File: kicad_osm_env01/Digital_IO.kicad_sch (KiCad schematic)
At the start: 4 parts

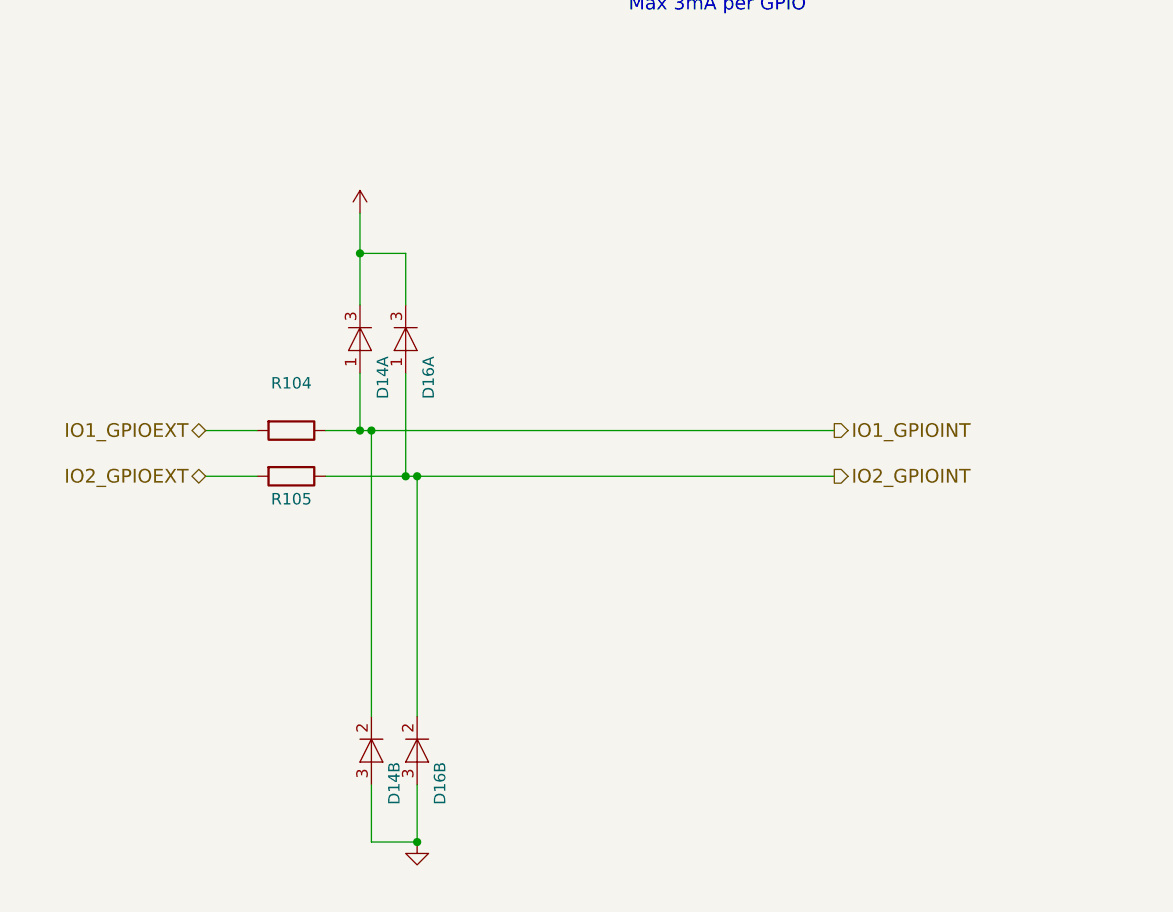
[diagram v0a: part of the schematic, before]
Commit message: added stml433 to schematic and carried out some mods
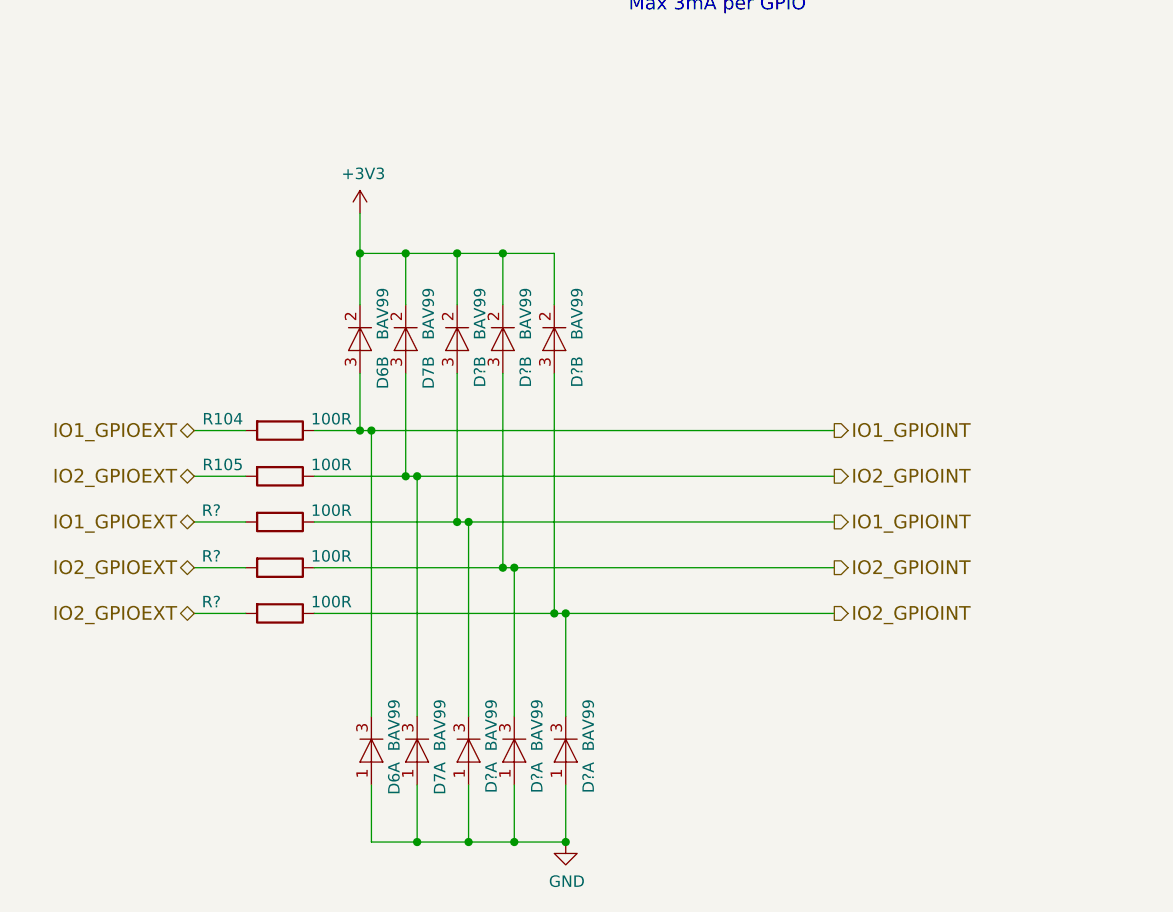
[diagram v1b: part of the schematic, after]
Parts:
- added D? (x6): BAV99, Package_TO_SOT_SMD:SOT-23, symbol OSM_env01-rescue:BAV99-Diode-ESP32-EVB_Rev_D-rescue
- added R? (x3): 100R, Resistor_SMD:R_0603_1608Metric, symbol OSM_env01-rescue:R-device-ESP32-EVB_Rev_D-rescue
- D6: renamed from D14; value (none) -> BAV99; footprint (none) -> Package_TO_SOT_SMD:SOT-23
- D7: renamed from D16; value (none) -> BAV99; footprint (none) -> Package_TO_SOT_SMD:SOT-23
- R104, R105: value (none) -> 100R; footprint (none) -> Resistor_SMD:R_0603_1608Metric
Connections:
- net +3V3: now also D6.2 (K), D7.2 (K), D?.2 (K), D?.2 (K), D?.2 (K); no longer D6.3 (K), D7.3 (K)
- net GND: now also D6.1 (A), D7.1 (A), D?.1 (A), D?.1 (A), D?.1 (A); no longer D6.3 (A), D7.3 (A)
- net IO1_GPIOEXT: now also R?.2
- net IO1_GPIOINT: now also D6.3 (A), D6.3 (K), D?.3 (A), D?.3 (K), R?.1; no longer D6.1 (A), D6.2 (K)
- net IO2_GPIOEXT: now also R?.2, R?.2
- net IO2_GPIOINT: now also D7.3 (A), D7.3 (K), D?.3 (A), D?.3 (A), D?.3 (K), D?.3 (K), R?.1, R?.1; no longer D7.1 (A), D7.2 (K)
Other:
- moved on the sheet: R104, R105

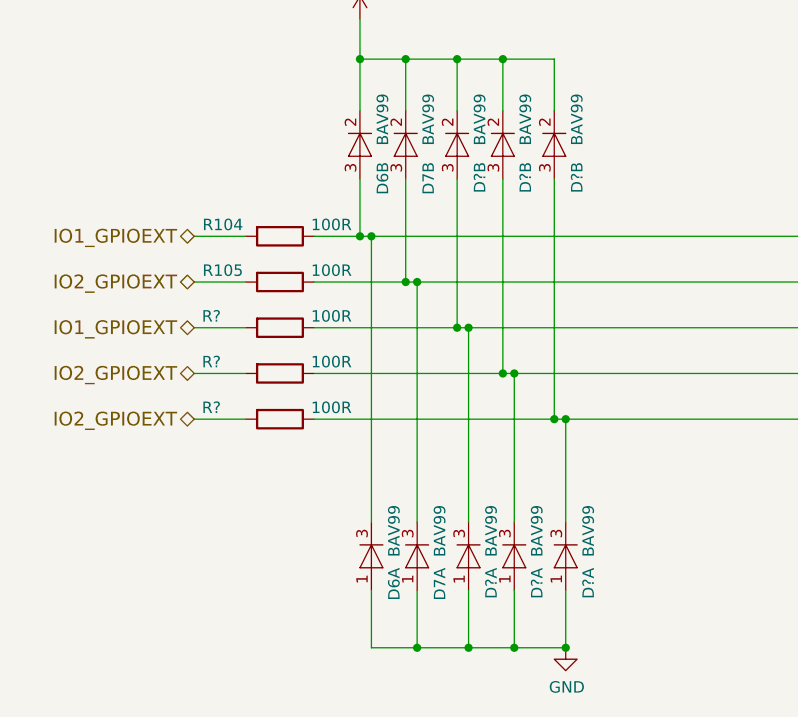
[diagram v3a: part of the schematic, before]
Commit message: added new battery charge ic u2
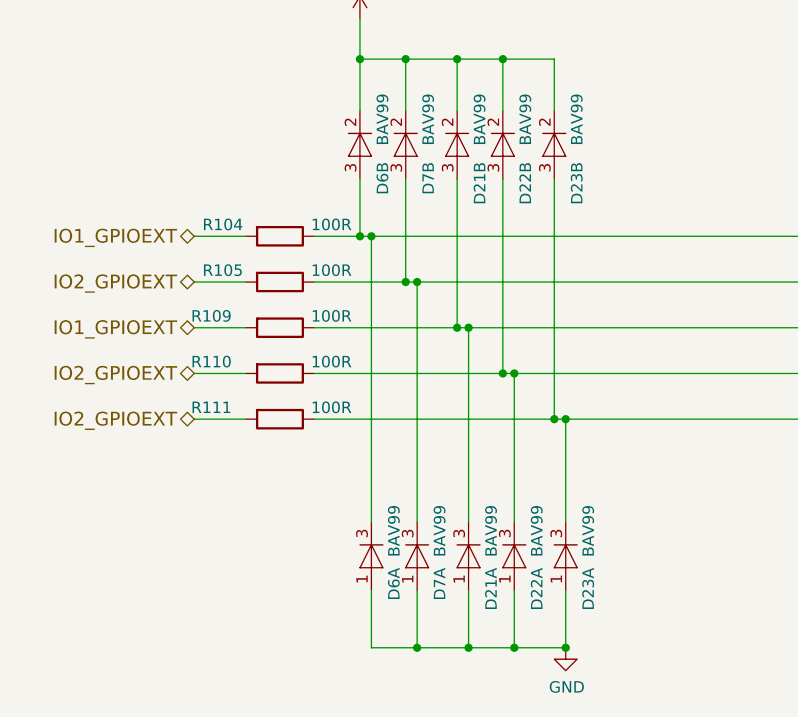
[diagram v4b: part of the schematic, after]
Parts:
- gave numbers to parts that had none: 6
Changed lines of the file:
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@@
   (title_block
     (title "Open Smart Monitor")
-    (date "2021-09-29")
-    (rev "B")
+    (date "2022-07-01")
+    (rev "C")
     (company "Devtank LTD")
     (comment 1 "Part No: 304-010")
@@
   (symbol (lib_id "OSM_env01:GND") (at 119.38 139.065 0) (unit 1)
     (in_bom yes) (on_board yes)
-    (property "Reference" "#PWR?" (id 0) (at 119.38 145.415 0)
+    (property "Reference" "#PWR075" (id 0) (at 119.38 145.415 0)
       (effects (font (size 1.27 1.27)) hide)
     )
@@
   (symbol (lib_id "OSM_env01-rescue:R-device-ESP32-EVB_Rev_D-rescue") (at 87.63 108.585 270) (unit 1)
     (in_bom yes) (on_board yes)
-    (property "Reference" "R?" (id 0) (at 80.01 107.315 90))
+    (property "Reference" "R110" (id 0) (at 80.01 107.315 90))
     (property "Value" "100R" (id 1) (at 93.345 107.315 90))
     (property "Footprint" "Resistor_SMD:R_0603_1608Metric" (id 2) (at 87.63 106.807 90)
@@
   (symbol (lib_id "OSM_env01-rescue:BAV99-Diode-ESP32-EVB_Rev_D-rescue") (at 112.395 83.185 270) (unit 2)
     (in_bom yes) (on_board yes)
-    (property "Reference" "D?" (id 0) (at 114.935 85.09 0)
+    (property "Reference" "D22" (id 0) (at 114.935 85.09 0)
       (effects (font (size 1.27 1.27)) (justify left))
     )
@@
   (symbol (lib_id "OSM_env01-rescue:R-device-ESP32-EVB_Rev_D-rescue") (at 87.63 113.665 270) (unit 1)
     (in_bom yes) (on_board yes)
-    (property "Reference" "R?" (id 0) (at 80.01 112.395 90))
+    (property "Reference" "R111" (id 0) (at 80.01 112.395 90))
     (property "Value" "100R" (id 1) (at 93.345 112.395 90))
     (property "Footprint" "Resistor_SMD:R_0603_1608Metric" (id 2) (at 87.63 111.887 90)
@@
   (symbol (lib_id "OSM_env01-rescue:BAV99-Diode-ESP32-EVB_Rev_D-rescue") (at 107.315 83.185 270) (unit 2)
     (in_bom yes) (on_board yes)
-    (property "Reference" "D?" (id 0) (at 109.855 85.09 0)
+    (property "Reference" "D21" (id 0) (at 109.855 85.09 0)
       (effects (font (size 1.27 1.27)) (justify left))
     )
@@
   (symbol (lib_id "OSM_env01-rescue:R-device-ESP32-EVB_Rev_D-rescue") (at 87.63 103.505 270) (unit 1)
     (in_bom yes) (on_board yes)
-    (property "Reference" "R?" (id 0) (at 80.01 102.235 90))
+    (property "Reference" "R109" (id 0) (at 80.01 102.235 90))
     (property "Value" "100R" (id 1) (at 93.345 102.235 90))
     (property "Footprint" "Resistor_SMD:R_0603_1608Metric" (id 2) (at 87.63 101.727 90)
@@
   (symbol (lib_id "OSM_env01-rescue:BAV99-Diode-ESP32-EVB_Rev_D-rescue") (at 108.585 128.905 270) (unit 1)
     (in_bom yes) (on_board yes)
-    (property "Reference" "D?" (id 0) (at 111.125 130.175 0)
+    (property "Reference" "D21" (id 0) (at 111.125 130.175 0)
       (effects (font (size 1.27 1.27)) (justify left))
     )
@@
   (symbol (lib_id "OSM_env01-rescue:BAV99-Diode-ESP32-EVB_Rev_D-rescue") (at 118.11 83.185 270) (unit 2)
     (in_bom yes) (on_board yes)
-    (property "Reference" "D?" (id 0) (at 120.65 85.09 0)
+    (property "Reference" "D23" (id 0) (at 120.65 85.09 0)
       (effects (font (size 1.27 1.27)) (justify left))
     )
@@
   (symbol (lib_id "OSM_env01-rescue:BAV99-Diode-ESP32-EVB_Rev_D-rescue") (at 119.38 128.905 270) (unit 1)
     (in_bom yes) (on_board yes)
-    (property "Reference" "D?" (id 0) (at 121.92 130.175 0)
+    (property "Reference" "D23" (id 0) (at 121.92 130.175 0)
       (effects (font (size 1.27 1.27)) (justify left))
     )
@@
   (symbol (lib_id "OSM_env01-rescue:BAV99-Diode-ESP32-EVB_Rev_D-rescue") (at 113.665 128.905 270) (unit 1)
     (in_bom yes) (on_board yes)
-    (property "Reference" "D?" (id 0) (at 116.205 130.175 0)
-      (effects (font (size 1.27 1.27)) (justify left))
-    )
+    (property "Reference" "D22" (id 0) (at 116.205 130.175 0)
+      (effects (font (size 1.27 1.27)) (justify left))
+    )

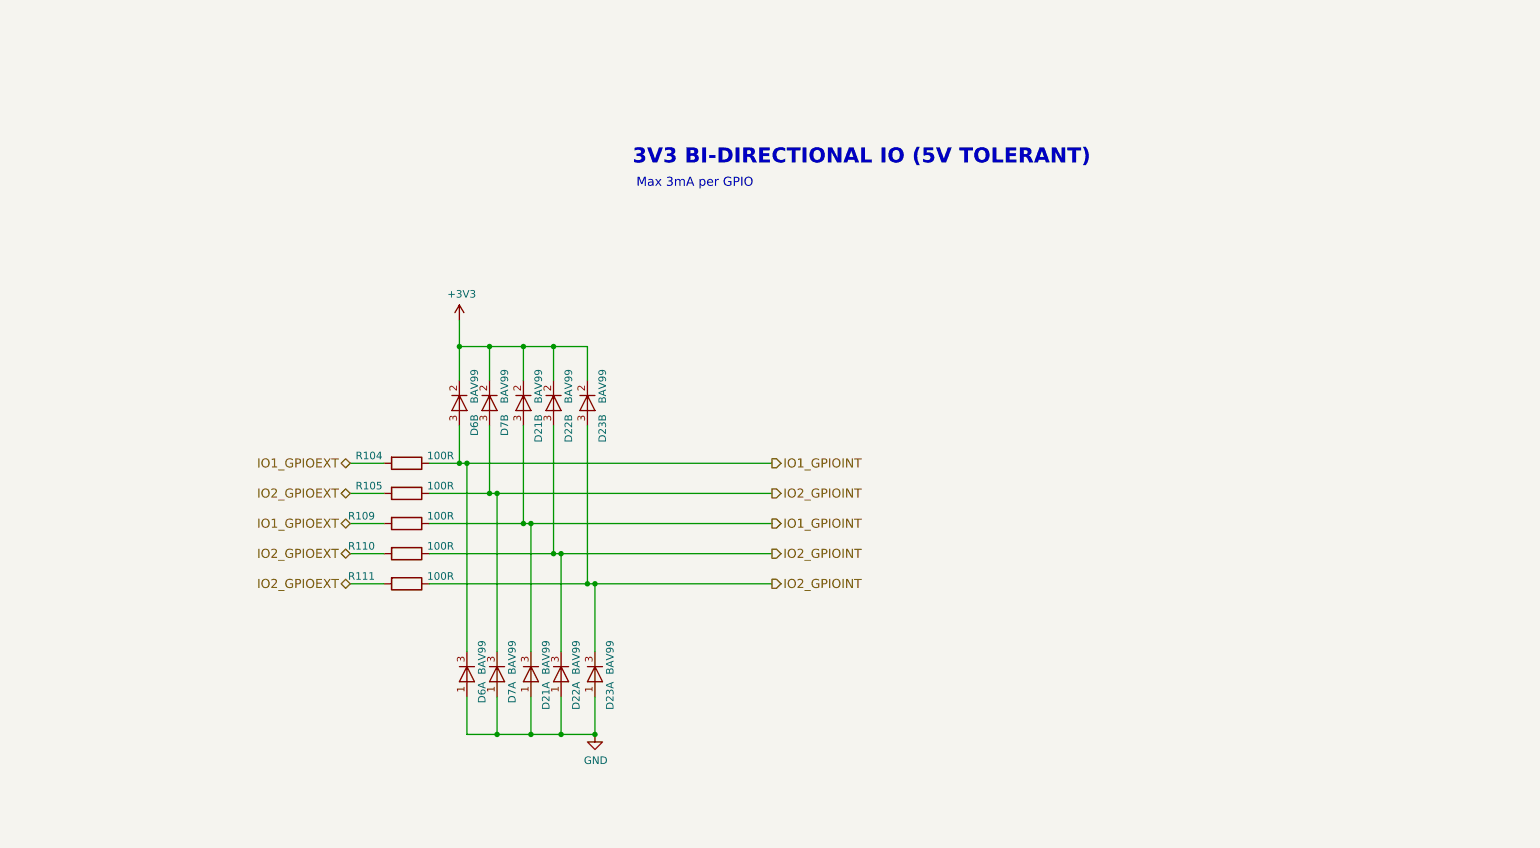
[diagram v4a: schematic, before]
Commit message: updated schematics and added rs232
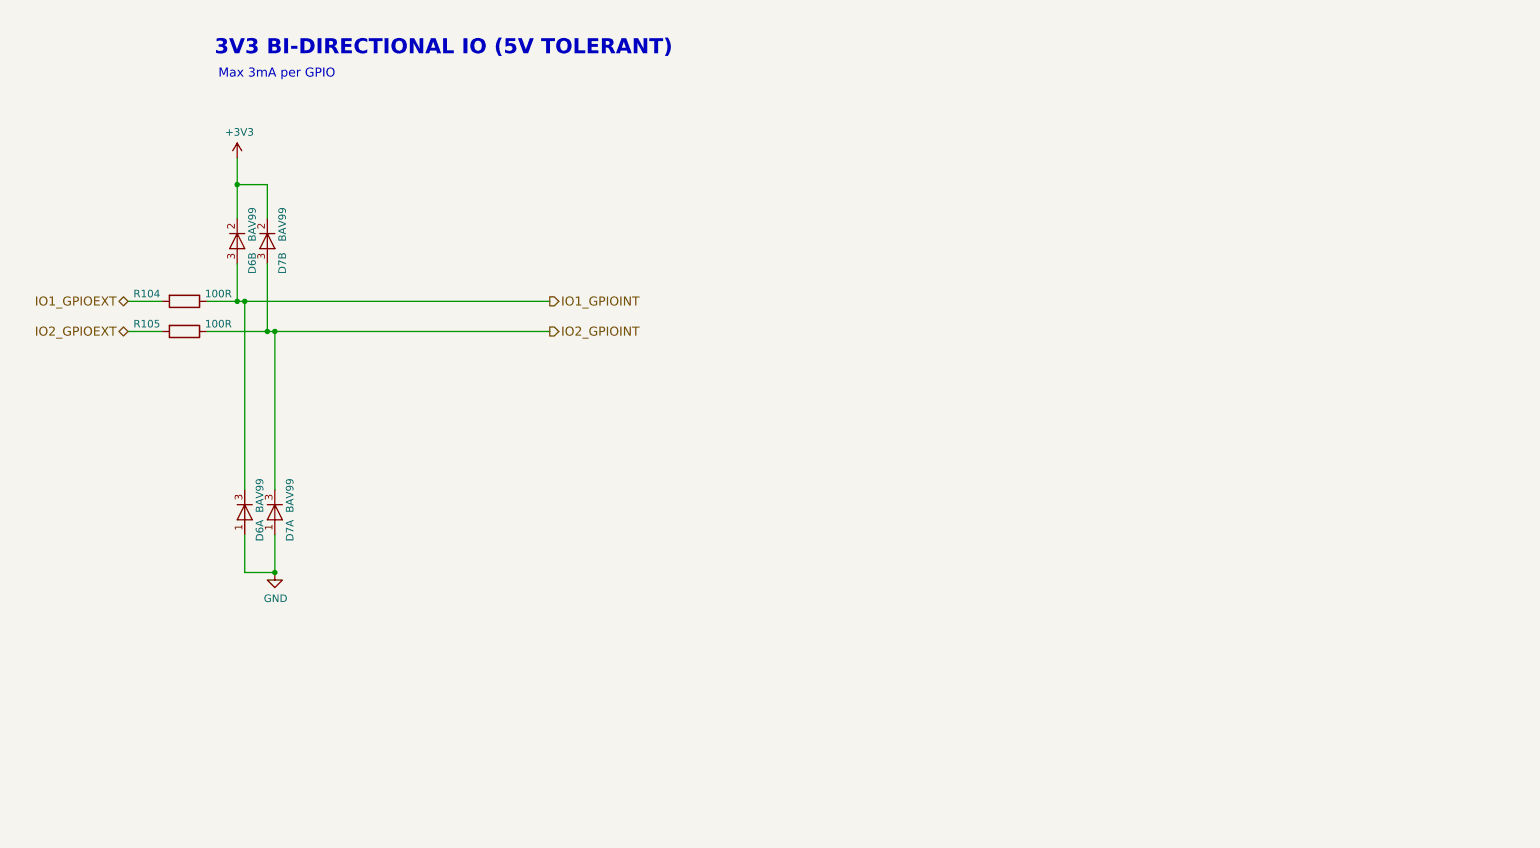
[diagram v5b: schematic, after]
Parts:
- removed D21, D22, D23: BAV99, Package_TO_SOT_SMD:SOT-23, symbol OSM_env01-rescue:BAV99-Diode-ESP32-EVB_Rev_D-rescue
- removed R109, R110, R111: 100R, Resistor_SMD:R_0603_1608Metric, symbol OSM_env01-rescue:R-device-ESP32-EVB_Rev_D-rescue
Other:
- moved on the sheet: D6A, D6B, D7A, D7B, R104, R105

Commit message: Schematics waiting review
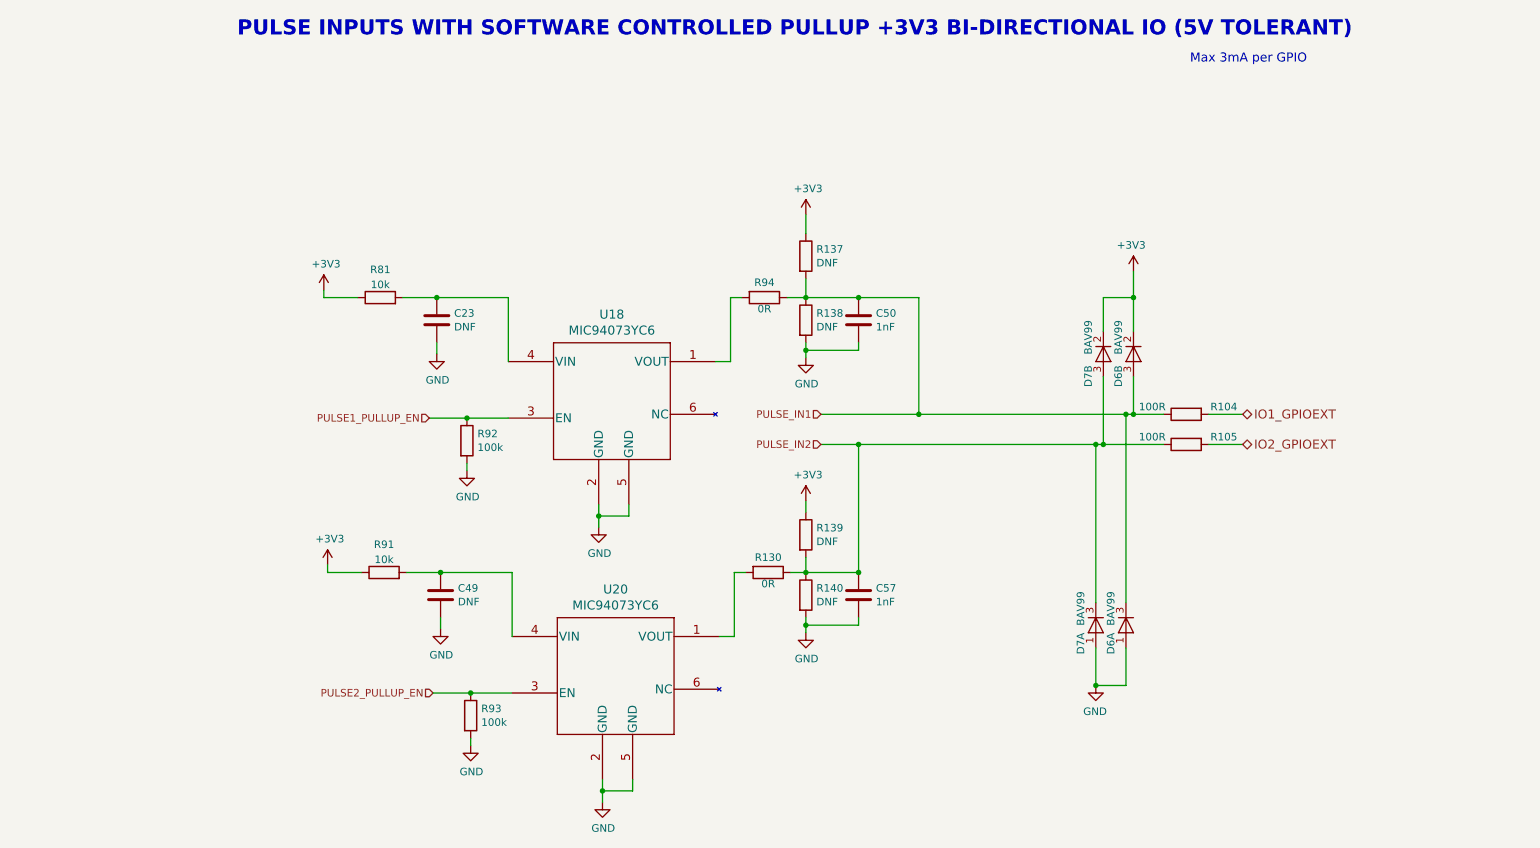
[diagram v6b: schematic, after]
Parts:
- added C23, C49: DNF, Capacitor_SMD:C_0603_1608Metric, symbol device:C
- added C50, C57: 1nF, Capacitor_SMD:C_0402_1005Metric, symbol device:C
- added R130, R94: 0R, Resistor_SMD:R_0603_1608Metric, symbol device:R
- added R137, R138, R139, R140: DNF, Resistor_SMD:R_0603_1608Metric, symbol OSM_env01-rescue:R-device-ESP32-EVB_Rev_D-rescue
- added R81, R91: 10k, symbol Device:R
- added R92, R93: 100k, Resistor_SMD:R_0603_1608Metric, symbol device:R
- added U18, U20: MIC94073YC6, Package_TO_SOT_SMD:SOT-363_SC-70-6, symbol Devtank:MIC94073YC6
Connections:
- net +3V3: now also R137.1, R139.1, R81.1, R91.1
- net GND: now also C23.2, C49.2, C50.2, C57.2, R138.2, R140.2, R92.2, R93.2, U18.2 (GND), U18.5 (GND), U20.2 (GND), U20.5 (GND)
- net IO1_GPIOINT renamed PULSE_IN1
- net PULSE_IN1: now also C50.1, R137.2, R138.1, R94.1
- net IO2_GPIOINT renamed PULSE_IN2
- net PULSE_IN2: now also C57.1, R130.1, R139.2, R140.1
- new net: C23.1, R81.2, U18.4 (VIN)
- new net: R94.2, U18.1 (VOUT)
- new net: C49.1, R91.2, U20.4 (VIN)
- new net: R130.2, U20.1 (VOUT)
- new net PULSE1_PULLUP_EN: R92.1, U18.3 (EN)
- new net PULSE2_PULLUP_EN: R93.1, U20.3 (EN)
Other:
- note added: "PULSE INPUTS WITH SOFTWARE CONTROLLED PULLUP +3V3 BI-DIRECTIONAL IO (5V TOLERANT)"
- note removed: "3V3 BI-DIRECTIONAL IO (5V TOLERANT)"
- moved on the sheet: D6A, D6B, D7A, D7B, R104, R105
